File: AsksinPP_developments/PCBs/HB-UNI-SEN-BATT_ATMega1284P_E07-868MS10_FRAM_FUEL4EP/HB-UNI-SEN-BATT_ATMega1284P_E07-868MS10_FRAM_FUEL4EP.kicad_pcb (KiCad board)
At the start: 2 copper layers, 75 x 75 mm, 63 parts, among them J1 Conn_01x02, J10 charge, J11 ePaper connector, J12 FTDI Debuger, J13 BME680, J2 Conn_01x02, J3 Conn_01x02, J4 Conn_01x02, J5 ISP Programmer, J6 SHT85, J7 AHT25, J8 AHT20+BMP280, J9 BME280/BMP280, Q1 IRLU024N, SW1 Config button, SW2 Reset button, U1 ATmega1284P-AU, U2 TPS61221DCK, U3 MB85RS2MTPF, U4 MB85RS2MTPF, Y1 8MHz

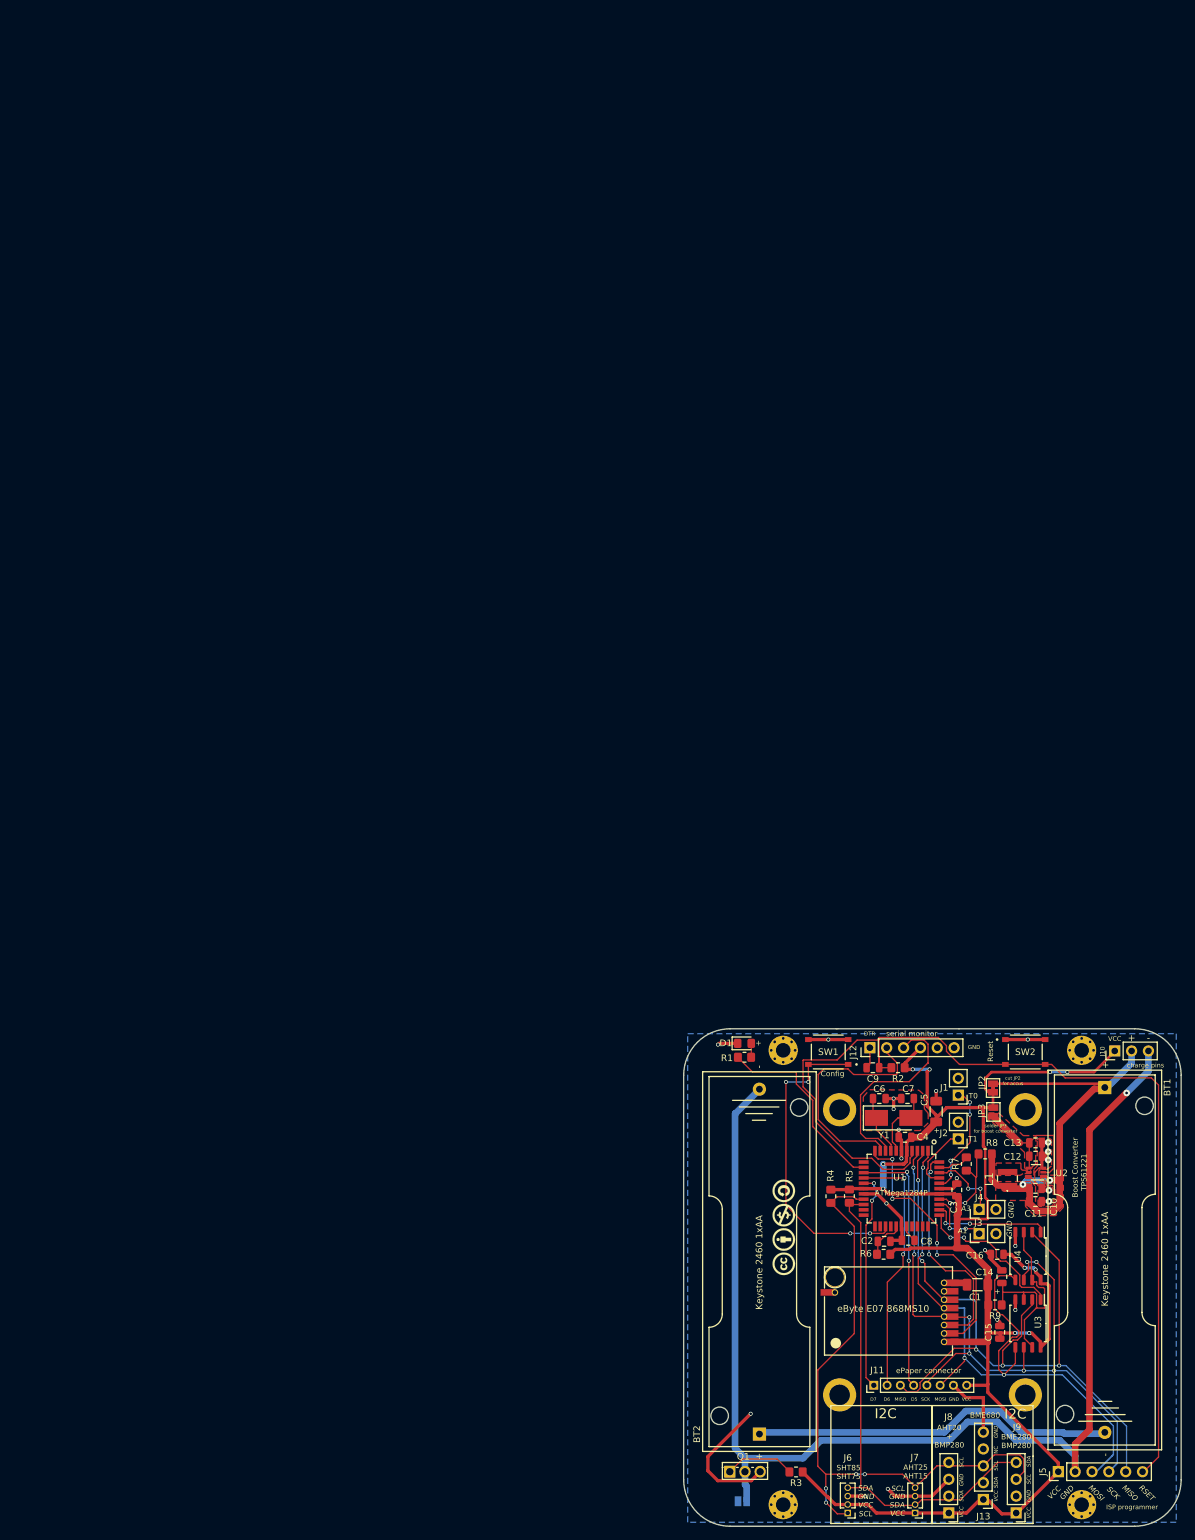
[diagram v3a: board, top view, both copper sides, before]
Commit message: PCBs: Fixes to ensure a proper production at JLCPCB, e.g. corrections of origins, rotations of assembled ICs etc.
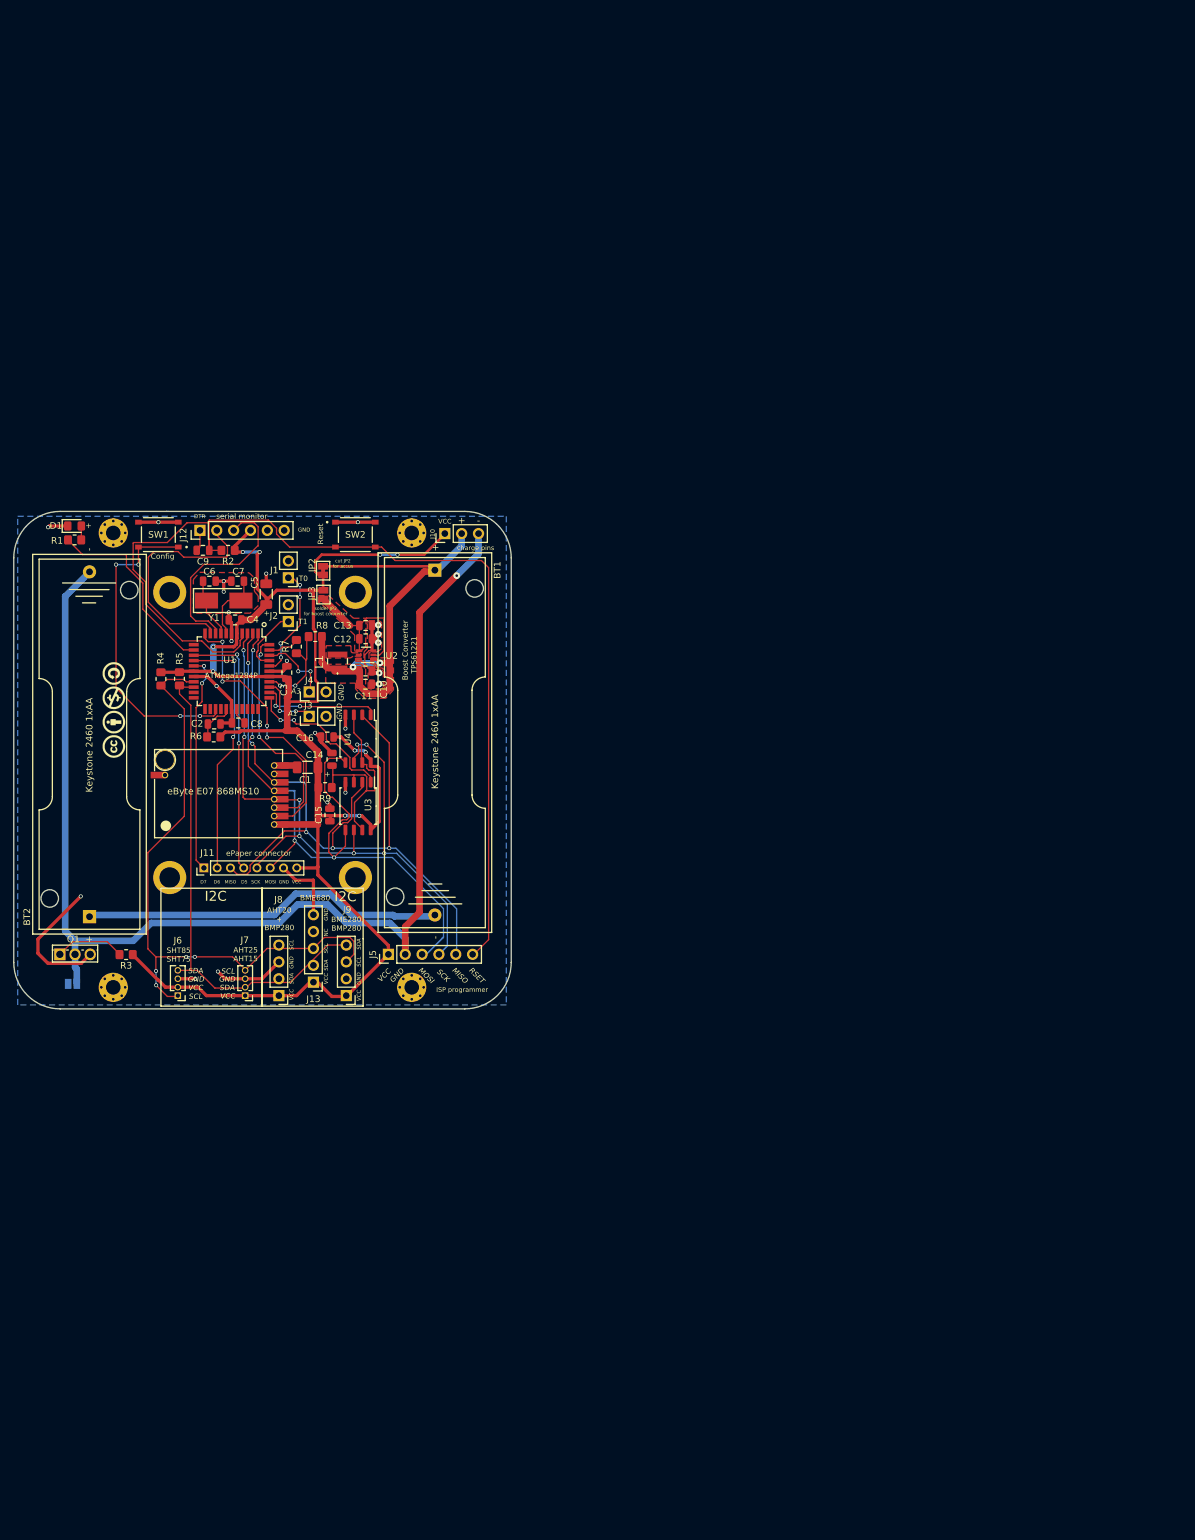
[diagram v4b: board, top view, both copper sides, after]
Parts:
- moved C1 127.6 mm to (44.3, 38.6)
- moved C4 127.6 mm to (33.4, 16.4)
- moved C7 127.6 mm to (33.7, 10.5)
- moved U1 127.6 mm to (32.8, 24.1)
- moved BT1 127.6 mm to (63.5, 8.86)
- moved BT2 127.6 mm to (11.4, 61.1)
- moved C10 127.6 mm to (53.0, 24.1)
- moved C11 127.6 mm to (53.0, 26.1)
- moved C12 127.6 mm to (53.1, 19.2)
- moved C13 127.6 mm to (53.1, 17.2)
- moved C14 127.6 mm to (48.0, 37.4)
- moved C15 127.6 mm to (47.7, 45.8)
- moved C16 127.6 mm to (47.3, 34.0)
- moved C2 127.6 mm to (30.2, 32.0)
- moved C3 127.6 mm to (41.2, 24.3)
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
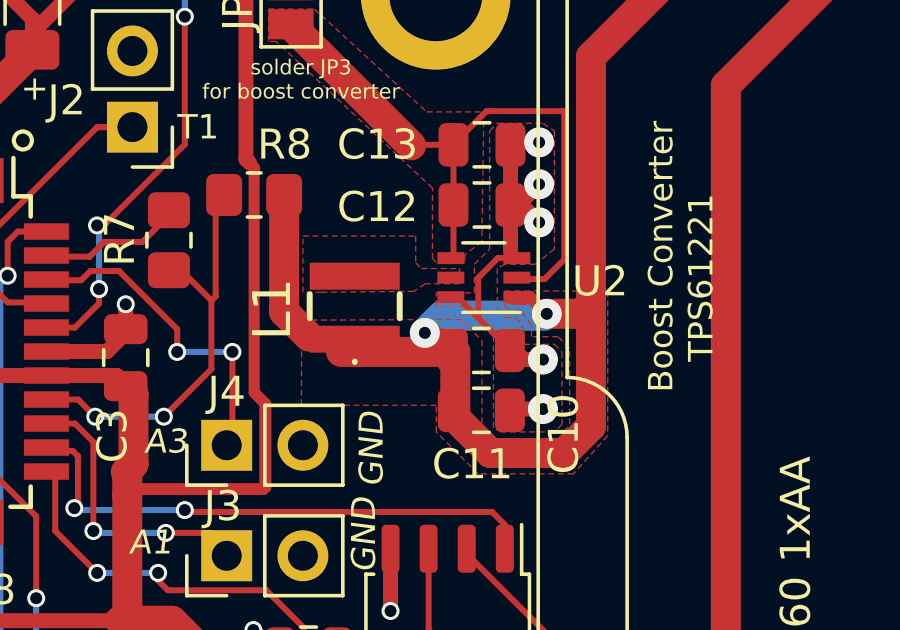
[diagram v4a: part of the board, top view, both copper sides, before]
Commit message: HB-UNI-SEN-BATT_ATMega1284P_E07-868MS10_FUEL4EP and HB-UNI-SEN-BATT_ATMega1284P_E07-868MS10_FRAM_FUEL4EP: Fix of wrong connection of EN pin of TPS61221 boost converter
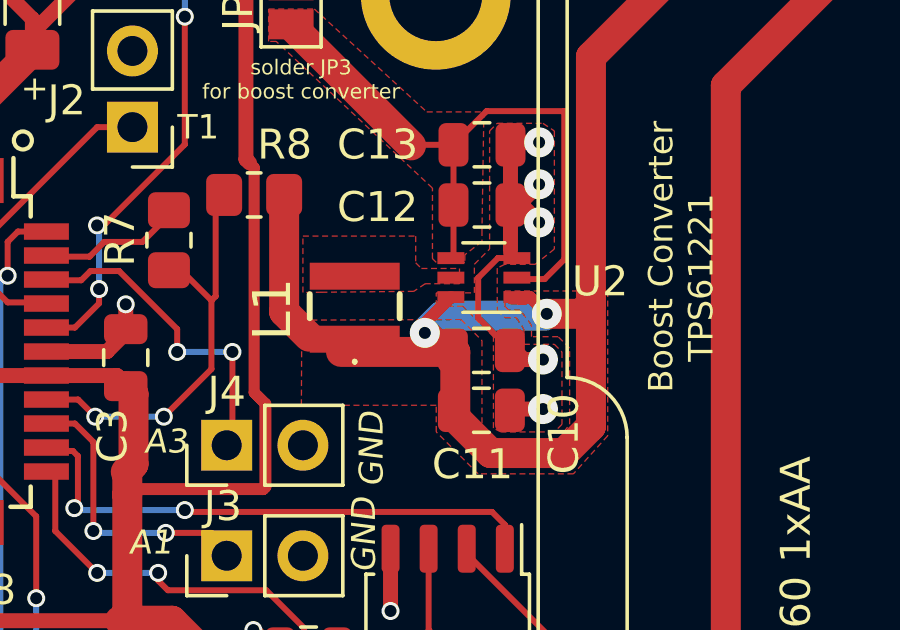
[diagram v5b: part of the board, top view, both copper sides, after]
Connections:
- U2 pad 6: GND -> /plusBAT
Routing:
- net /plusBAT: track 71.6 -> 73.2 mm
- net GND: track 109.6 -> 108.7 mm
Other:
- board text added: "Version 1.4 - 07/2023 (KiCAD 6)"
- board text removed: "Version 1.3 - 07/2023 (KiCAD 6)"
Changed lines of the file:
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@@
   (title_block
     (title "HB-UNI-SEN-BATT_ATMega1284P_E07-868MS10_FRAM_FUEL4EP")
-    (date "2023-07-24")
-    (rev "1.3")
+    (date "2023-08-15")
+    (rev "1.4")
     (company "FUEL4EP")
   )
@@
     (property "Sheetname" "")
     (property "TYPE" "0")
-    (attr through_hole exclude_from_pos_files exclude_from_bom)
+    (attr through_hole exclude_from_pos_files)
     (fp_text reference "J3" (at 1.651 -0.127) (layer "F.SilkS")
       (effects (font (size 1 1) (thickness 0.15)))
@@
     (property "Sheetname" "")
     (property "TYPE" "0")
-    (attr through_hole exclude_from_pos_files exclude_from_bom)
+    (attr through_hole exclude_from_pos_files)
     (fp_text reference "J4" (at 1.778 0) (layer "F.SilkS")
       (effects (font (size 1 1) (thickness 0.15)))
@@
     (property "Sheetname" "")
     (property "TYPE" "0")
-    (attr through_hole exclude_from_pos_files exclude_from_bom)
+    (attr through_hole exclude_from_pos_files)
     (fp_text reference "J5" (at 0 -2.33 90) (layer "F.SilkS")
       (effects (font (size 1 1) (thickness 0.15)))
@@
     (property "Sheetname" "")
     (property "TYPE" "0")
-    (attr through_hole exclude_from_pos_files exclude_from_bom)
+    (attr through_hole exclude_from_pos_files)
     (fp_text reference "J10" (at -0.0635 -1.8415 90) (layer "F.SilkS")
       (effects (font (size 0.7 0.7) (thickness 0.15)))
@@
     (property "Sheetname" "")
     (property "TYPE" "0")
-    (attr through_hole exclude_from_pos_files exclude_from_bom)
+    (attr through_hole exclude_from_pos_files)
     (fp_text reference "J8" (at 0.0635 14.478) (layer "F.SilkS")
       (effects (font (size 1 1) (thickness 0.15)))
@@
     (property "Sheetname" "")
     (property "TYPE" "0")
-    (attr through_hole exclude_from_pos_files exclude_from_bom)
+    (attr through_hole exclude_from_pos_files)
     (fp_text reference "J12" (at -0.6985 -2.5146 90) (layer "F.SilkS")
       (effects (font (size 1 1) (thickness 0.15)))
@@
       (net 42 "Net-(L1-Pad2)") (pinfunction "L") (pintype "power_in"))
     (pad "6" smd rect (at 1.1 -0.65 180) (size 0.9 0.4) (layers "F.Cu" "F.Paste" "F.Mask")
-      (net 1 "GND") (pinfunction "EN") (pintype "input"))
+      (net 18 "/plusBAT") (pinfunction "EN") (pintype "input"))
     (model "${KICAD6_3DMODEL_DIR}/Package_TO_SOT_SMD.3dshapes/SOT-363_SC-70-6.wrl"
       (offset (xyz 0 0 0))
@@
     (property "Sheetname" "")
     (property "TYPE" "0")
-    (attr through_hole exclude_from_pos_files exclude_from_bom)
+    (attr through_hole exclude_from_pos_files)
     (fp_text reference "J6" (at 0 8.3155) (layer "F.SilkS")
       (effects (font (size 1 1) (thickness 0.15)))
@@
     (property "Sheetname" "")
     (property "TYPE" "0")
-    (attr through_hole exclude_from_pos_files exclude_from_bom)
+    (attr through_hole exclude_from_pos_files)
     (fp_text reference "J9" (at -0.127 12.951) (layer "F.SilkS")
       (effects (font (size 1 1) (thickness 0.15)))
@@
     (property "Sheetname" "")
     (property "TYPE" "0")
-    (attr through_hole exclude_from_pos_files exclude_from_bom)
+    (attr through_hole exclude_from_pos_files)
     (fp_text reference "J7" (at 0.0635 8.382) (layer "F.SilkS")
       (effects (font (size 1 1) (thickness 0.15)))
@@
     (property "Sheetname" "")
     (property "TYPE" "0")
-    (attr through_hole exclude_from_pos_files exclude_from_bom)
+    (attr through_hole exclude_from_pos_files)
     (fp_text reference "J13" (at 0 -2.54) (layer "F.SilkS")
       (effects (font (size 1 1) (thickness 0.15)))
@@
     (effects (font (size 1 1) (thickness 0.2)) (justify left mirror))
   )
-  (gr_text "Version 1.3 - 07/2023 (KiCAD 6)\n" (at 6.2515 5.058 90) (layer "B.SilkS")
+  (gr_text "Version 1.4 - 07/2023 (KiCAD 6)\n" (at 6.2515 5.058 90) (layer "B.SilkS")
     (effects (font (size 1.2 1.2) (thickness 0.2)) (justify left mirror))
   )
@@
   (segment (start 30.56315 26.32165) (end 30.572 26.3305) (width 0.5) (layer "F.Cu") (net 1))
   (segment (start 54.448 24.362) (end 54.194 24.108) (width 0.5) (layer "F.Cu") (net 1))
-  (segment (start 52.23796 22.27896) (end 52.924 22.965) (width 0.2) (layer "F.Cu") (net 1))
   (segment (start 52.924 22.965) (end 54.067 24.108) (width 0.2) (layer "F.Cu") (net 1))
   (segment (start 3.648 64.494) (end 10.0996 58.0424) (width 0.5) (layer "F.Cu") (net 1))
@@
   (segment (start 56.336732 22.864428) (end 56.6832 22.51796) (width 0.2) (layer "F.Cu") (net 18))
   (segment (start 52.162 24.108) (end 48.352 24.108) (width 1) (layer "F.Cu") (net 18))
+  (segment (start 51.146 23.15) (end 52.0145 22.2815) (width 0.4) (layer "F.Cu") (net 18))
   (segment (start 61.89 9.06) (end 56.6832 14.2668) (width 1) (layer "F.Cu") (net 18))
   (segment (start 56.5562 22.33) (end 56.6832 22.203) (width 0.4) (layer "F.Cu") (net 18))
@@
   (segment (start 46.4564 22.7712) (end 47.2852 23.6) (width 1) (layer "F.Cu") (net 18))
   (segment (start 56.36316 22.838) (end 56.6832 22.51796) (width 1) (layer "F.Cu") (net 18))
+  (segment (start 51.146 23.473) (end 51.146 23.15) (width 0.4) (layer "F.Cu") (net 18))
   (segment (start 53.33717 27.47865) (end 52.162 26.30348) (width 1) (layer "F.Cu") (net 18))
   (segment (start 63.49 9.06) (end 61.89 9.06) (width 1) (layer "F.Cu") (net 18))

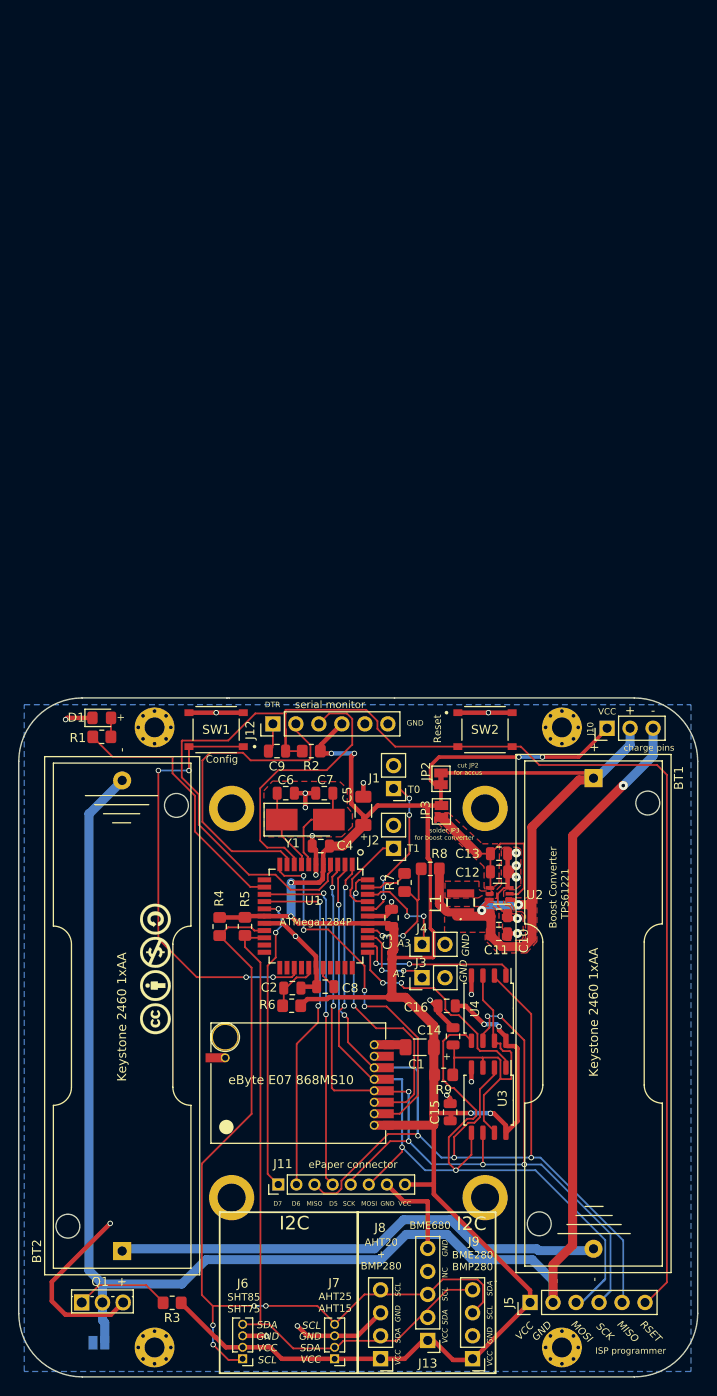
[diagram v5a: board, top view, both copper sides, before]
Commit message: PCBs: moved origin to lower left corner in order to fit to JLCPCB's scheme
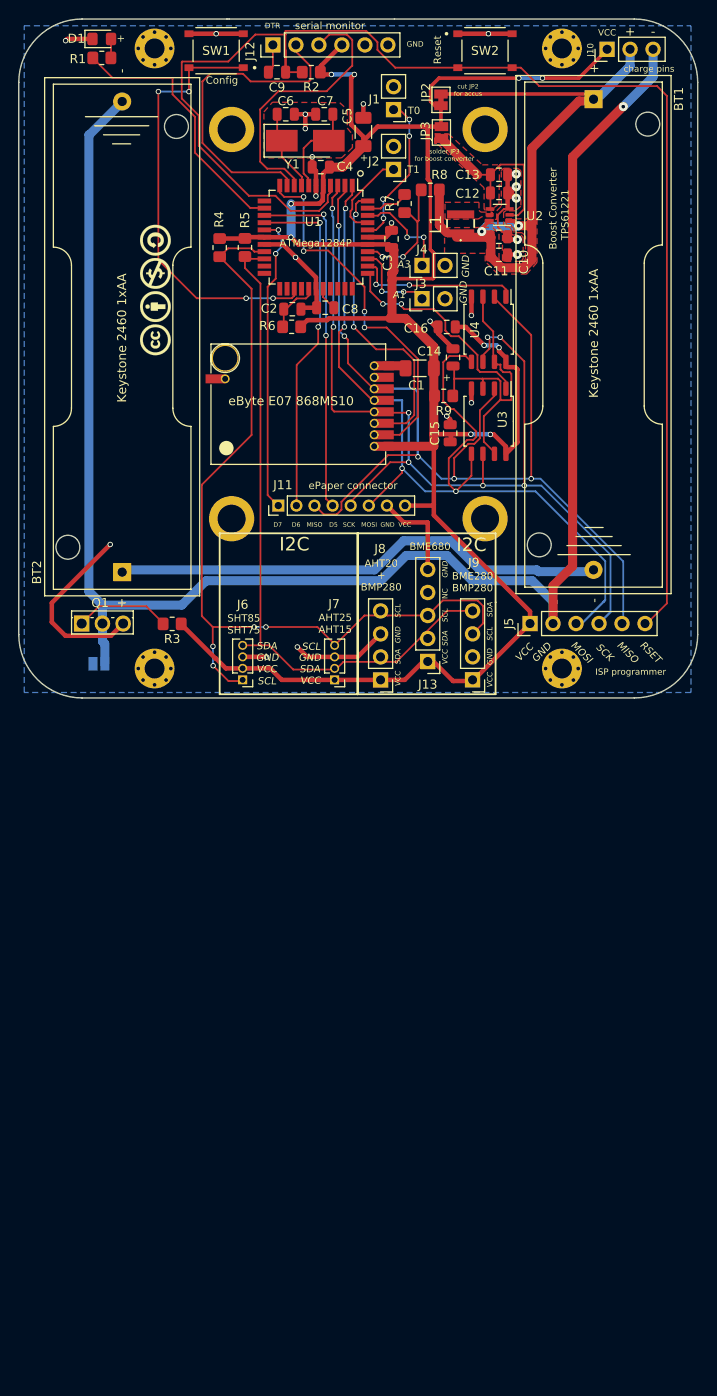
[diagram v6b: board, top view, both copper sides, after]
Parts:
- moved BT1 75.0 mm to (63.5, -66.1)
- moved BT2 75.0 mm to (11.4, -13.9)
- moved C1 75.0 mm to (44.3, -36.4)
- moved C10 75.0 mm to (53.0, -50.9)
- moved C11 75.0 mm to (53.0, -48.9)
- moved C12 75.0 mm to (53.1, -55.8)
- moved C13 75.0 mm to (53.1, -57.8)
- moved C14 75.0 mm to (48.0, -37.6)
- moved C15 75.0 mm to (47.7, -29.2)
- moved C16 75.0 mm to (47.3, -41.0)
- moved C2 75.0 mm to (30.2, -43.0)
- moved C3 75.0 mm to (41.2, -50.7)
- moved C4 75.0 mm to (33.4, -58.6)
- moved C5 75.0 mm to (38.1, -62.5)
- moved C6 75.0 mm to (29.5, -64.5)
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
